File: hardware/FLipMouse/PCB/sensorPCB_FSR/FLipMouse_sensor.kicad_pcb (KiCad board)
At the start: 2 copper layers, 32 x 32 mm, 9 parts, among them J1 Conn_02x05_Odd_Even, J2 FSR1, J3 FSR1, J4 FSR2, J5 FSR2, J6 FSR3, J7 FSR3, J8 FSR4, J9 FSR4

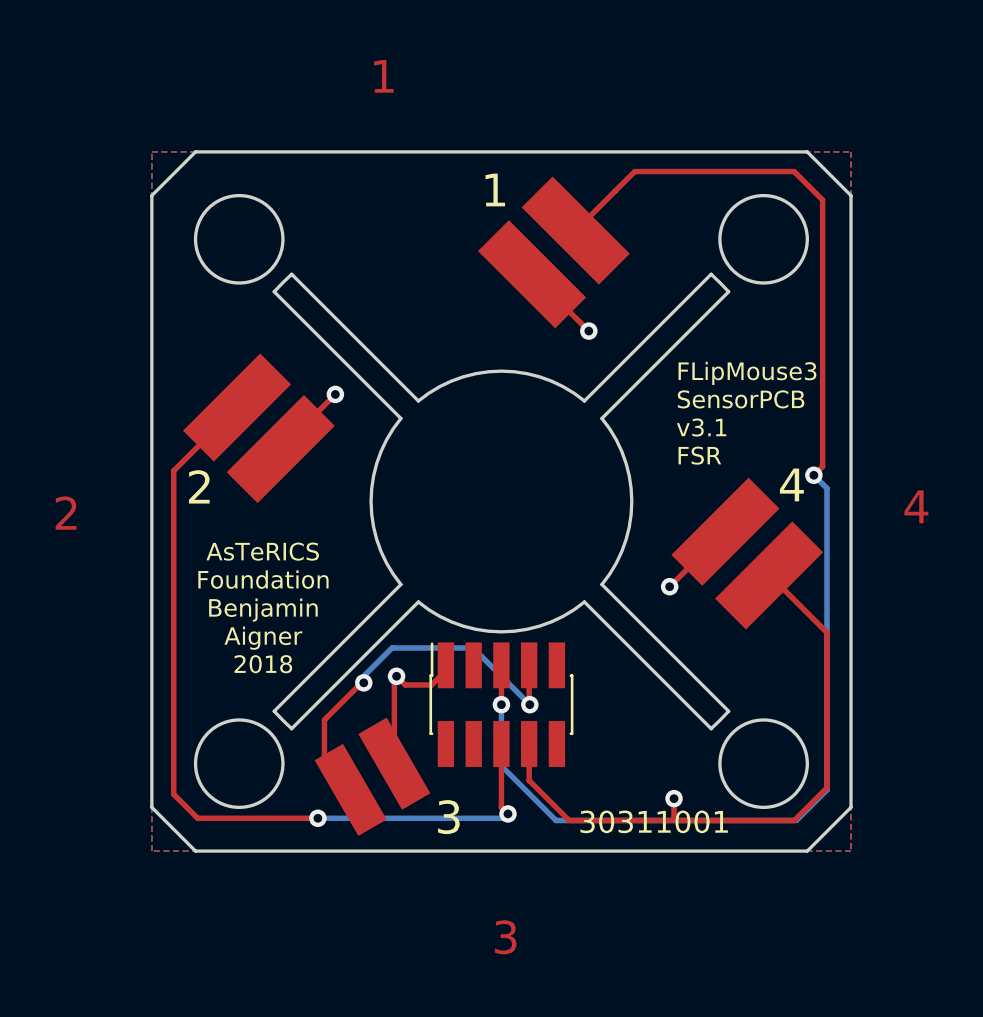
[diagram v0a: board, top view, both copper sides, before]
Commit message: Added MEMS microphone to sensor PCB for voice recognition. Added production information
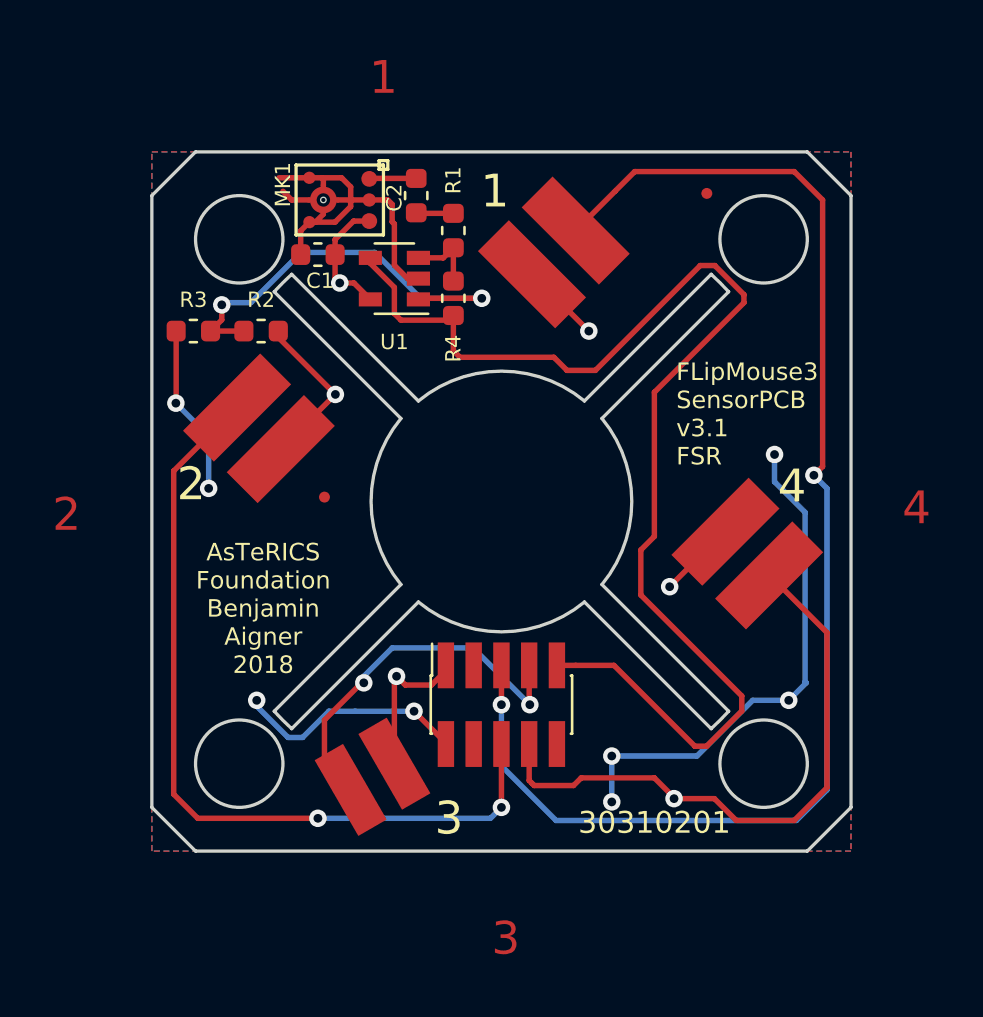
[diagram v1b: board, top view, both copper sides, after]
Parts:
- added C1: 100nF, Capacitor_SMD:C_0603_1608Metric, F.Cu at (107.6, 102.7)
- added C2: 4.7uF, Capacitor_SMD:C_0603_1608Metric, F.Cu at (112.1, 100.0)
- added FID1: Fiducial, Fiducial:Fiducial_0.5mm_Dia_1mm_Outer, F.Cu at (107.9, 113.8)
- added FID2: Fiducial, Fiducial:Fiducial_0.5mm_Dia_1mm_Outer, F.Cu at (125.4, 99.9)
- added MK1: SPU0410LR5H, SPU0410:SPU0410LR5H_6_3.76x3mm, F.Cu at (108.6, 100.2)
- added R1: 10k, Resistor_SMD:R_0603_1608Metric, F.Cu at (113.8, 101.6)
- added R2: 100k, Resistor_SMD:R_0603_1608Metric, F.Cu at (105.0, 106.2)
- added R3: 100k, Resistor_SMD:R_0603_1608Metric, F.Cu at (101.9, 106.2)
- added R4: 100k, Resistor_SMD:R_0603_1608Metric, F.Cu at (113.8, 104.7)
- added U1: LMV321, Package_TO_SOT_SMD:SOT-23-5, F.Cu at (111.1, 103.8)
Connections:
- J1 pad 10: Net-(J1-Pad10) -> (no net)
- J1 pad 3: Net-(J1-Pad3) -> (no net)
- J1 pad 4: Net-(J1-Pad4) -> (no net)
- J1 pad 9: Net-(J1-Pad9) -> /EXT1
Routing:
- net GNDD: track 0.00 -> 59.4 mm, vias 0 -> 8
- net /EXT1: track 0.00 -> 57.3 mm
- net Net-(R2-Pad1): track 0.00 -> 19.6 mm, vias 0 -> 2
- net 3V3: track 18.4 -> 28.1 mm, vias 4 -> 5
- net Net-(R1-Pad1): track 0.00 -> 3.32 mm
- net Net-(C2-Pad2): track 0.00 -> 2.16 mm
- net Net-(C2-Pad1): track 0.00 -> 1.71 mm
- net /4: track 28.5 -> 27.8 mm
- net /2: track 38.1 -> 37.5 mm
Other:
- board text added: "30310201"
- board text removed: "30311001"
